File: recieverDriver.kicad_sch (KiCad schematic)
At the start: 19 parts, among them U1 MC33079, U4 MC33079

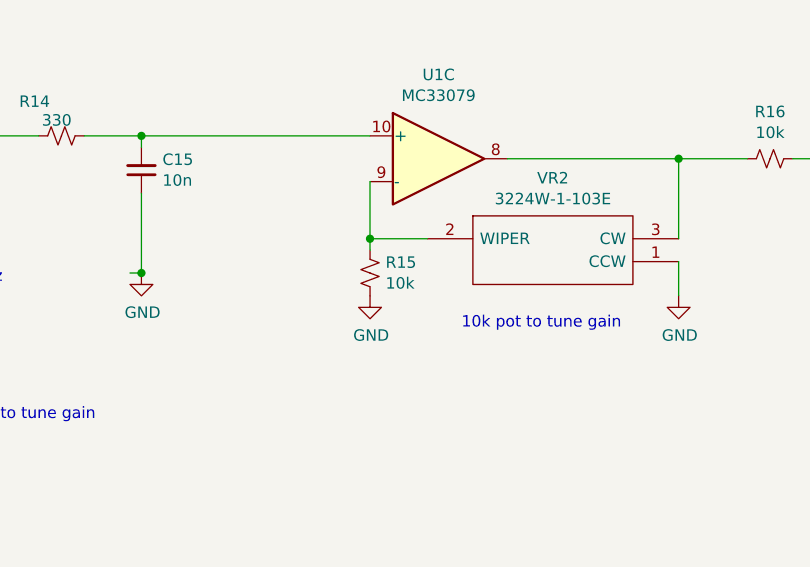
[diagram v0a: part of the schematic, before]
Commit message: yeah I think this one is better, also updated resistor values after lab work
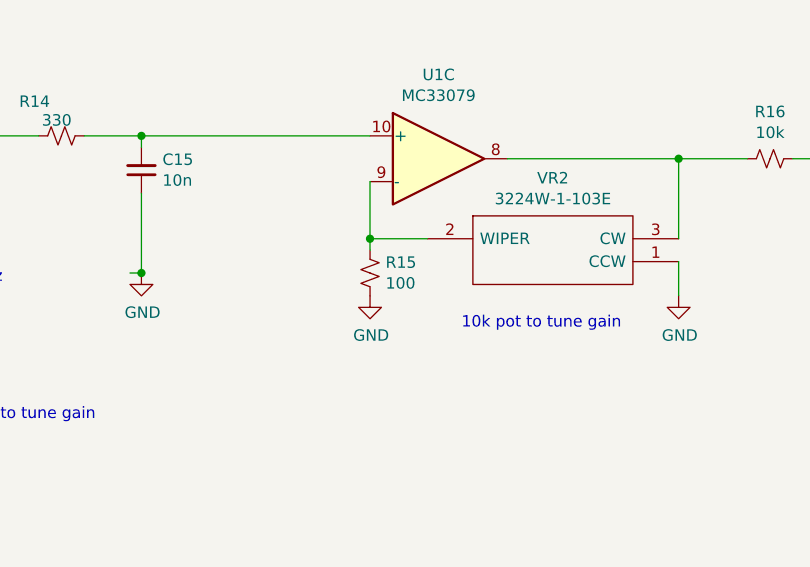
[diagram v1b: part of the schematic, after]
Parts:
- R15: value 10k -> 100
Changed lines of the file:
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@@
       (effects (font (size 1.27 1.27)) (justify left))
     )
-    (property "Value" "10k" (id 1) (at 126.1872 106.553 0)
+    (property "Value" "100" (id 1) (at 126.1872 106.553 0)
       (effects (font (size 1.27 1.27)) (justify left))
     )

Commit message: this draft has gone to justin
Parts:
- removed D5, D6: 1N5819, Diode_THT:D_DO-41_SOD81_P10.16mm_Horizontal, symbol Diode:1N5819
- added D5, D6: B5819W.SL, SamacSys_Parts:B5819WSL, symbol SamacSys_Parts:B5819W.SL
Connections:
- net 3.3V: now also D5.1
- net GND: now also D6.2
- net sigOut: now also D5.2, D6.1
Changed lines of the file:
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@@
   )
   (no_connect (at 81.28 130.81))
-  (wire (pts (xy 209.55 101.6) (xy 209.55 105.41))
-    (stroke (width 0) (type default) (color 0 0 0 0))
-  )
   (wire (pts (xy 124.46 101.6) (xy 130.81 101.6))
-    (stroke (width 0) (type default) (color 0 0 0 0))
-  )
-  (wire (pts (xy 222.25 101.6) (xy 222.25 107.95))
     (stroke (width 0) (type default) (color 0 0 0 0))
   )
@@
     )
   )
-  (global_label "3.3V" (shape input) (at 209.55 105.41 270) (fields_autoplaced)
+  (global_label "3.3V" (shape input) (at 209.55 109.22 270) (fields_autoplaced)
     (effects (font (size 1.27 1.27)) (justify right))
-    (property "Intersheet References" "${INTERSHEET_REFS}" (id 0) (at 0 0 0)
+    (property "Intersheet References" "${INTERSHEET_REFS}" (id 0) (at 0 3.81 0)
       (effects (font (size 1.27 1.27)) hide)
     )
@@
     (pin "1")
   )
-  (symbol (lib_id "Diode:1N5819") (at 209.55 97.79 90) (unit 1)
-    (in_bom yes) (on_board yes)
-    (property "Reference" "D5" (id 0) (at 211.5566 96.6216 90)
-      (effects (font (size 1.27 1.27)) (justify right))
-    )
-    (property "Value" "1N5819" (id 1) (at 211.5566 98.933 90)
-      (effects (font (size 1.27 1.27)) (justify right))
-    )
-    (property "Footprint" "Diode_THT:D_DO-41_SOD81_P10.16mm_Horizontal" (id 2) (at 213.995 97.79 0)
-      (effects (font (size 1.27 1.27)) hide)
-    )
-    (property "Datasheet" "http://www.vishay.com/docs/88525/1n5817.pdf" (id 3) (at 209.55 97.79 0)
-      (effects (font (size 1.27 1.27)) hide)
-    )
-    (pin "1")
-    (pin "2")
-  )
-  (symbol (lib_id "Diode:1N5819") (at 222.25 97.79 270) (unit 1)
-    (in_bom yes) (on_board yes)
-    (property "Reference" "D6" (id 0) (at 227.33 96.52 90)
-      (effects (font (size 1.27 1.27)) (justify right))
-    )
-    (property "Value" "1N5819" (id 1) (at 231.14 99.06 90)
-      (effects (font (size 1.27 1.27)) (justify right))
-    )
-    (property "Footprint" "Diode_THT:D_DO-41_SOD81_P10.16mm_Horizontal" (id 2) (at 217.805 97.79 0)
-      (effects (font (size 1.27 1.27)) hide)
-    )
-    (property "Datasheet" "http://www.vishay.com/docs/88525/1n5817.pdf" (id 3) (at 222.25 97.79 0)
-      (effects (font (size 1.27 1.27)) hide)
-    )
-    (pin "1")
-    (pin "2")
-  )
-  (symbol (lib_id "power:GND") (at 222.25 107.95 0) (unit 1)
-    (in_bom yes) (on_board yes)
-    (property "Reference" "#PWR032" (id 0) (at 222.25 114.3 0)
-      (effects (font (size 1.27 1.27)) hide)
-    )
-    (property "Value" "GND" (id 1) (at 222.377 112.3442 0))
-    (property "Footprint" "" (id 2) (at 222.25 107.95 0)
-      (effects (font (size 1.27 1.27)) hide)
-    )
-    (property "Datasheet" "" (id 3) (at 222.25 107.95 0)
+  (symbol (lib_id "power:GND") (at 222.25 109.22 0) (unit 1)
+    (in_bom yes) (on_board yes)
+    (property "Reference" "#PWR032" (id 0) (at 222.25 115.57 0)
+      (effects (font (size 1.27 1.27)) hide)
+    )
+    (property "Value" "GND" (id 1) (at 222.377 113.6142 0))
+    (property "Footprint" "" (id 2) (at 222.25 109.22 0)
+      (effects (font (size 1.27 1.27)) hide)
+    )
+    (property "Datasheet" "" (id 3) (at 222.25 109.22 0)
       (effects (font (size 1.27 1.27)) hide)
     )
@@
       (effects (font (size 1.27 1.27)) (justify left) hide)
     )
+    (pin "1")
+    (pin "2")
+  )
+  (symbol (lib_id "SamacSys_Parts:B5819W.SL") (at 222.25 91.44 270) (unit 1)
+    (in_bom yes) (on_board yes) (fields_autoplaced)
+    (property "Reference" "D6" (id 0) (at 225.552 100.7653 90)
+      (effects (font (size 1.27 1.27)) (justify left))
+    )
+    (property "Value" "B5819W.SL" (id 1) (at 225.552 103.3022 90)
+      (effects (font (size 1.27 1.27)) (justify left))
+    )
+    (property "Footprint" "SamacSys_Parts:B5819WSL" (id 2) (at 226.06 104.14 0)
+      (effects (font (size 1.27 1.27)) (justify left) hide)
+    )
+    (property "Datasheet" "https://file.elecfans.com/web1/M00/8A/32/pIYBAFyLiveAInCMAAthN3CVBXo401.pdf?filename=1505718310707869662.pdf" (id 3) (at 223.52 104.14 0)
+      (effects (font (size 1.27 1.27)) (justify left) hide)
+    )
+    (property "Description" "SOD-123 Plastic-Encapsulate Diodes" (id 4) (at 220.98 104.14 0)
+      (effects (font (size 1.27 1.27)) (justify left) hide)
+    )
+    (property "Height" "1.25" (id 5) (at 218.44 104.14 0)
+      (effects (font (size 1.27 1.27)) (justify left) hide)
+    )
+    (property "RS Part Number" "" (id 6) (at 215.9 104.14 0)
+      (effects (font (size 1.27 1.27)) (justify left) hide)
+    )
+    (property "RS Price/Stock" "" (id 7) (at 213.36 104.14 0)
+      (effects (font (size 1.27 1.27)) (justify left) hide)
+    )
+    (property "Manufacturer_Name" "1-Avel" (id 8) (at 210.82 104.14 0)
+      (effects (font (size 1.27 1.27)) (justify left) hide)
+    )
+    (property "Manufacturer_Part_Number" "B5819W.SL" (id 9) (at 208.28 104.14 0)
+      (effects (font (size 1.27 1.27)) (justify left) hide)
+    )
+    (pin "1")
+    (pin "2")
+  )
+  (symbol (lib_id "SamacSys_Parts:B5819W.SL") (at 209.55 111.76 90) (unit 1)
+    (in_bom yes) (on_board yes) (fields_autoplaced)
+    (property "Reference" "D5" (id 0) (at 212.852 100.7653 90)
+      (effects (font (size 1.27 1.27)) (justify right))
+    )
+    (property "Value" "B5819W.SL" (id 1) (at 212.852 103.3022 90)
+      (effects (font (size 1.27 1.27)) (justify right))
+    )
+    (property "Footprint" "SamacSys_Parts:B5819WSL" (id 2) (at 205.74 99.06 0)
+      (effects (font (size 1.27 1.27)) (justify left) hide)
+    )
+    (property "Datasheet" "https://file.elecfans.com/web1/M00/8A/32/pIYBAFyLiveAInCMAAthN3CVBXo401.pdf?filename=1505718310707869662.pdf" (id 3) (at 208.28 99.06 0)
+      (effects (font (size 1.27 1.27)) (justify left) hide)
+    )
+    (property "Description" "SOD-123 Plastic-Encapsulate Diodes" (id 4) (at 210.82 99.06 0)
+      (effects (font (size 1.27 1.27)) (justify left) hide)
+    )
+    (property "Height" "1.25" (id 5) (at 213.36 99.06 0)
+      (effects (font (size 1.27 1.27)) (justify left) hide)
+    )
+    (property "RS Part Number" "" (id 6) (at 215.9 99.06 0)
+      (effects (font (size 1.27 1.27)) (justify left) hide)
+    )
+    (property "RS Price/Stock" "" (id 7) (at 218.44 99.06 0)
+      (effects (font (size 1.27 1.27)) (justify left) hide)
+    )
+    (property "Manufacturer_Name" "1-Avel" (id 8) (at 220.98 99.06 0)
+      (effects (font (size 1.27 1.27)) (justify left) hide)
+    )
+    (property "Manufacturer_Part_Number" "B5819W.SL" (id 9) (at 223.52 99.06 0)
+      (effects (font (size 1.27 1.27)) (justify left) hide)
+    )

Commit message: updated and sent to Justin
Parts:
- removed D5, D6: B5819W.SL, SamacSys_Parts:B5819WSL, symbol SamacSys_Parts:B5819W.SL
- added D5, D6: 1N5819, Diode_THT:D_DO-41_SOD81_P10.16mm_Horizontal, symbol Diode:1N5819
- R15: value 100 -> 10k
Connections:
- net 3.3V: now also D5.1 (K)
- net GND: now also D6.2 (A)
- net sigOut: now also D5.2 (A), D6.1 (K)
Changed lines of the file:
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@@
   )
   (no_connect (at 81.28 130.81))
+  (wire (pts (xy 209.55 101.6) (xy 209.55 105.41))
+    (stroke (width 0) (type default) (color 0 0 0 0))
+  )
   (wire (pts (xy 124.46 101.6) (xy 130.81 101.6))
+    (stroke (width 0) (type default) (color 0 0 0 0))
+  )
+  (wire (pts (xy 222.25 101.6) (xy 222.25 107.95))
     (stroke (width 0) (type default) (color 0 0 0 0))
   )
@@
     )
   )
-  (global_label "3.3V" (shape input) (at 209.55 109.22 270) (fields_autoplaced)
+  (global_label "3.3V" (shape input) (at 209.55 105.41 270) (fields_autoplaced)
     (effects (font (size 1.27 1.27)) (justify right))
-    (property "Intersheet References" "${INTERSHEET_REFS}" (id 0) (at 0 3.81 0)
+    (property "Intersheet References" "${INTERSHEET_REFS}" (id 0) (at 0 0 0)
       (effects (font (size 1.27 1.27)) hide)
     )
@@
       (effects (font (size 1.27 1.27)) (justify left))
     )
-    (property "Value" "100" (id 1) (at 126.1872 106.553 0)
+    (property "Value" "10k" (id 1) (at 126.1872 106.553 0)
       (effects (font (size 1.27 1.27)) (justify left))
     )
@@
     (pin "1")
   )
-  (symbol (lib_id "power:GND") (at 222.25 109.22 0) (unit 1)
-    (in_bom yes) (on_board yes)
-    (property "Reference" "#PWR032" (id 0) (at 222.25 115.57 0)
-      (effects (font (size 1.27 1.27)) hide)
-    )
-    (property "Value" "GND" (id 1) (at 222.377 113.6142 0))
-    (property "Footprint" "" (id 2) (at 222.25 109.22 0)
-      (effects (font (size 1.27 1.27)) hide)
-    )
-    (property "Datasheet" "" (id 3) (at 222.25 109.22 0)
+  (symbol (lib_id "Diode:1N5819") (at 209.55 97.79 90) (unit 1)
+    (in_bom yes) (on_board yes)
+    (property "Reference" "D5" (id 0) (at 211.5566 96.6216 90)
+      (effects (font (size 1.27 1.27)) (justify right))
+    )
+    (property "Value" "1N5819" (id 1) (at 211.5566 98.933 90)
+      (effects (font (size 1.27 1.27)) (justify right))
+    )
+    (property "Footprint" "Diode_THT:D_DO-41_SOD81_P10.16mm_Horizontal" (id 2) (at 213.995 97.79 0)
+      (effects (font (size 1.27 1.27)) hide)
+    )
+    (property "Datasheet" "http://www.vishay.com/docs/88525/1n5817.pdf" (id 3) (at 209.55 97.79 0)
+      (effects (font (size 1.27 1.27)) hide)
+    )
+    (pin "1")
+    (pin "2")
+  )
+  (symbol (lib_id "Diode:1N5819") (at 222.25 97.79 270) (unit 1)
+    (in_bom yes) (on_board yes)
+    (property "Reference" "D6" (id 0) (at 227.33 96.52 90)
+      (effects (font (size 1.27 1.27)) (justify right))
+    )
+    (property "Value" "1N5819" (id 1) (at 231.14 99.06 90)
+      (effects (font (size 1.27 1.27)) (justify right))
+    )
+    (property "Footprint" "Diode_THT:D_DO-41_SOD81_P10.16mm_Horizontal" (id 2) (at 217.805 97.79 0)
+      (effects (font (size 1.27 1.27)) hide)
+    )
+    (property "Datasheet" "http://www.vishay.com/docs/88525/1n5817.pdf" (id 3) (at 222.25 97.79 0)
+      (effects (font (size 1.27 1.27)) hide)
+    )
+    (pin "1")
+    (pin "2")
+  )
+  (symbol (lib_id "power:GND") (at 222.25 107.95 0) (unit 1)
+    (in_bom yes) (on_board yes)
+    (property "Reference" "#PWR032" (id 0) (at 222.25 114.3 0)
+      (effects (font (size 1.27 1.27)) hide)
+    )
+    (property "Value" "GND" (id 1) (at 222.377 112.3442 0))
+    (property "Footprint" "" (id 2) (at 222.25 107.95 0)
+      (effects (font (size 1.27 1.27)) hide)
+    )
+    (property "Datasheet" "" (id 3) (at 222.25 107.95 0)
       (effects (font (size 1.27 1.27)) hide)
     )
@@
       (effects (font (size 1.27 1.27)) (justify left) hide)
     )
-    (pin "1")
-    (pin "2")
-  )
-  (symbol (lib_id "SamacSys_Parts:B5819W.SL") (at 222.25 91.44 270) (unit 1)
-    (in_bom yes) (on_board yes) (fields_autoplaced)
-    (property "Reference" "D6" (id 0) (at 225.552 100.7653 90)
-      (effects (font (size 1.27 1.27)) (justify left))
-    )
-    (property "Value" "B5819W.SL" (id 1) (at 225.552 103.3022 90)
-      (effects (font (size 1.27 1.27)) (justify left))
-    )
-    (property "Footprint" "SamacSys_Parts:B5819WSL" (id 2) (at 226.06 104.14 0)
-      (effects (font (size 1.27 1.27)) (justify left) hide)
-    )
-    (property "Datasheet" "https://file.elecfans.com/web1/M00/8A/32/pIYBAFyLiveAInCMAAthN3CVBXo401.pdf?filename=1505718310707869662.pdf" (id 3) (at 223.52 104.14 0)
-      (effects (font (size 1.27 1.27)) (justify left) hide)
-    )
-    (property "Description" "SOD-123 Plastic-Encapsulate Diodes" (id 4) (at 220.98 104.14 0)
-      (effects (font (size 1.27 1.27)) (justify left) hide)
-    )
-    (property "Height" "1.25" (id 5) (at 218.44 104.14 0)
-      (effects (font (size 1.27 1.27)) (justify left) hide)
-    )
-    (property "RS Part Number" "" (id 6) (at 215.9 104.14 0)
-      (effects (font (size 1.27 1.27)) (justify left) hide)
-    )
-    (property "RS Price/Stock" "" (id 7) (at 213.36 104.14 0)
-      (effects (font (size 1.27 1.27)) (justify left) hide)
-    )
-    (property "Manufacturer_Name" "1-Avel" (id 8) (at 210.82 104.14 0)
-      (effects (font (size 1.27 1.27)) (justify left) hide)
-    )
-    (property "Manufacturer_Part_Number" "B5819W.SL" (id 9) (at 208.28 104.14 0)
-      (effects (font (size 1.27 1.27)) (justify left) hide)
-    )
-    (pin "1")
-    (pin "2")
-  )
-  (symbol (lib_id "SamacSys_Parts:B5819W.SL") (at 209.55 111.76 90) (unit 1)
-    (in_bom yes) (on_board yes) (fields_autoplaced)
-    (property "Reference" "D5" (id 0) (at 212.852 100.7653 90)
-      (effects (font (size 1.27 1.27)) (justify right))
-    )
-    (property "Value" "B5819W.SL" (id 1) (at 212.852 103.3022 90)
-      (effects (font (size 1.27 1.27)) (justify right))
-    )
-    (property "Footprint" "SamacSys_Parts:B5819WSL" (id 2) (at 205.74 99.06 0)
-      (effects (font (size 1.27 1.27)) (justify left) hide)
-    )
-    (property "Datasheet" "https://file.elecfans.com/web1/M00/8A/32/pIYBAFyLiveAInCMAAthN3CVBXo401.pdf?filename=1505718310707869662.pdf" (id 3) (at 208.28 99.06 0)
-      (effects (font (size 1.27 1.27)) (justify left) hide)
-    )
-    (property "Description" "SOD-123 Plastic-Encapsulate Diodes" (id 4) (at 210.82 99.06 0)
-      (effects (font (size 1.27 1.27)) (justify left) hide)
-    )
-    (property "Height" "1.25" (id 5) (at 213.36 99.06 0)
-      (effects (font (size 1.27 1.27)) (justify left) hide)
-    )
-    (property "RS Part Number" "" (id 6) (at 215.9 99.06 0)
-      (effects (font (size 1.27 1.27)) (justify left) hide)
-    )
-    (property "RS Price/Stock" "" (id 7) (at 218.44 99.06 0)
-      (effects (font (size 1.27 1.27)) (justify left) hide)
-    )
-    (property "Manufacturer_Name" "1-Avel" (id 8) (at 220.98 99.06 0)
-      (effects (font (size 1.27 1.27)) (justify left) hide)
-    )
-    (property "Manufacturer_Part_Number" "B5819W.SL" (id 9) (at 223.52 99.06 0)
-      (effects (font (size 1.27 1.27)) (justify left) hide)
-    )
-    (pin "1")
-    (pin "2")
+    (pin "2")
+    (pin "1")
   )
 )
